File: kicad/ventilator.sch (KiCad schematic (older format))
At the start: 44 parts, among them J1 Conn_01x02, J2 Conn_01x02, J3 Conn_01x02, J4 Conn_01x02, J5 Conn_01x02, J6 Conn_01x02, Q1 IRLIZ44NPBF, Q2 IRLIZ44NPBF, Q3 IRLIZ44NPBF, Q4 IRLIZ44NPBF, Q5 IRLIZ44NPBF, Q6 IRLIZ44NPBF

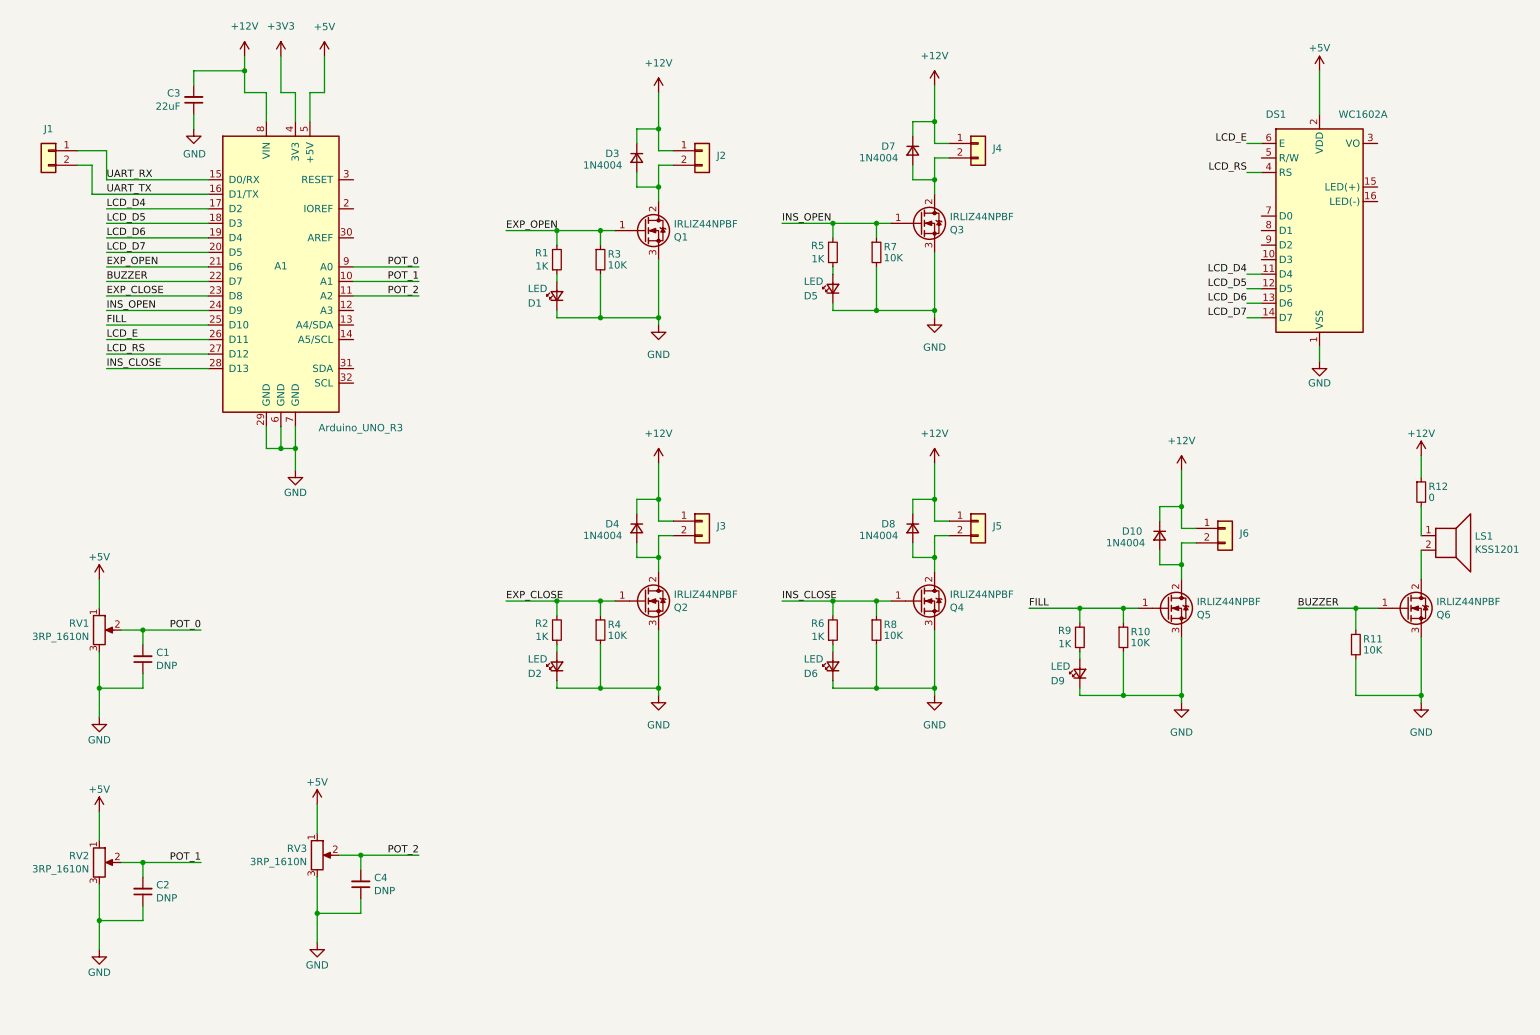
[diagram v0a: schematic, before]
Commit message: modifies schematic with new pin mapping
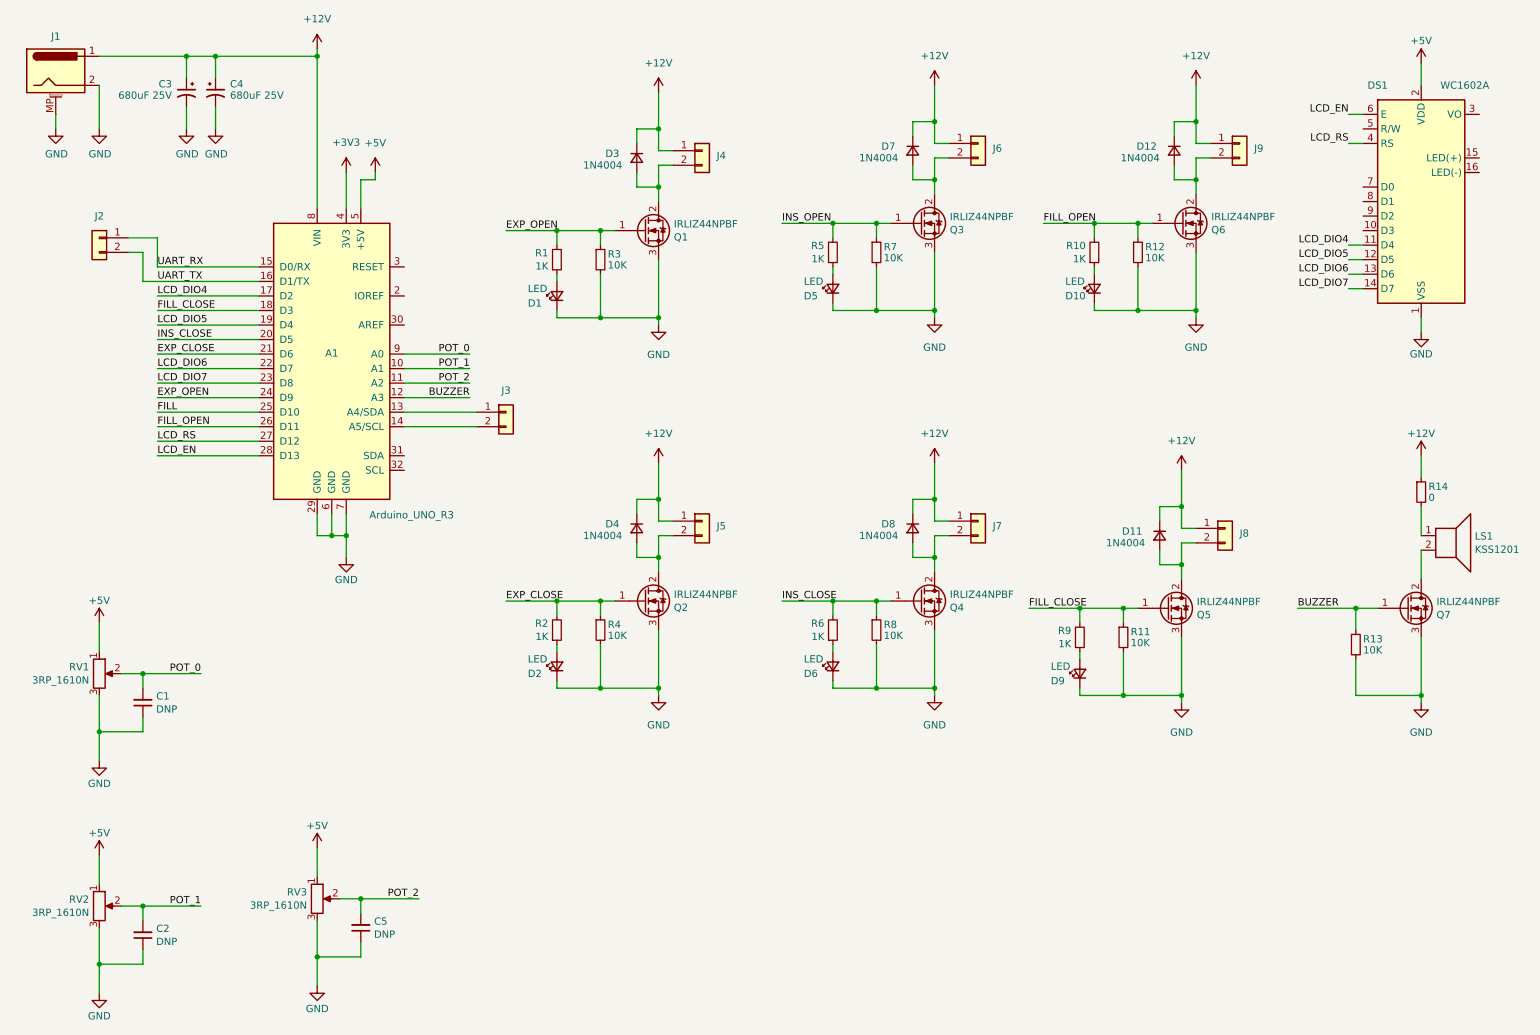
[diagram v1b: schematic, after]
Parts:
- removed C3: 22uF, Capacitor_THT:C_Radial_D6.3mm_H5.0mm_P2.50mm, symbol Device:C_Small
- added C3, C4: 680uF 25V, Capacitor_THT:CP_Radial_D10.0mm_P5.00mm, symbol Device:CP1_Small
- added D10: LED, LED_THT:LED_D5.0mm, symbol Device:LED_Small
- added D12: 1N4004, Diode_THT:D_DO-41_SOD81_P7.62mm_Horizontal, symbol Device:D_Small
- added J1: Barrel_Jack_MountingPin, symbol Connector:Barrel_Jack_MountingPin
- added J3, J9: Conn_01x02, Connector_Phoenix_MSTB:PhoenixContact_MSTBA_2,5_2-G-5,08_1x02_P5.08mm_Horizontal, symbol Connector_Generic:Conn_01x02
- added Q6: IRLIZ44NPBF, Package_TO_SOT_THT:TO-220-3_Vertical, symbol Device:Q_NMOS_GDS
- added R10: 1K, Resistor_THT:R_Axial_DIN0207_L6.3mm_D2.5mm_P7.62mm_Horizontal, symbol Device:R_Small
- added R12: 10K, Resistor_THT:R_Axial_DIN0207_L6.3mm_D2.5mm_P7.62mm_Horizontal, symbol Device:R_Small
- renumbered C4 to C5, D10 to D11, J1 to J2, J2 to J4, J3 to J5, J4 to J6, J5 to J7, J6 to J8, Q6 to Q7, R10 to R11, R11 to R13, R12 to R14
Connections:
- net +12V: now also C3.1, C4.1, D12.1 (K), J1.1, J9.1 (Pin_1)
- net BUZZER: now also A1.12 (A3); no longer A1.22 (D7)
- net EXP_CLOSE: now also A1.21 (D6); no longer A1.23 (D8)
- net EXP_OPEN: now also A1.24 (D9); no longer A1.21 (D6)
- net FILL: no longer Q5.1 (G), R11.1, R9.2
- net GND: now also C3.2, C4.2, D10.1 (K), J1.2, J1.MP (MountPin), Q6.3 (S), R12.2
- net INS_CLOSE: now also A1.20 (D5); no longer A1.28 (D13)
- net INS_OPEN: no longer A1.24 (D9)
- net at A1.13 (A4/SDA): now also J3.1 (Pin_1)
- net at A1.14 (A5/SCL): now also J3.2 (Pin_2)
- net LCD_D4 renamed LCD_DIO4
- net LCD_D5 renamed FILL_CLOSE
- net FILL_CLOSE: now also Q5.1 (G), R11.1, R9.2; no longer DS1.12 (D5)
- net LCD_D6 renamed LCD_DIO5
- net LCD_DIO5: now also DS1.12 (D5); no longer DS1.13 (D6)
- net LCD_D7 renamed LCD_DIO7
- net LCD_DIO7: now also A1.23 (D8); no longer A1.20 (D5)
- net LCD_E renamed FILL_OPEN
- net FILL_OPEN: now also Q6.1 (G), R10.2, R12.1; no longer DS1.6 (E)
- new net: D10.2 (A), R10.1
- new net: D12.2 (A), J9.2 (Pin_2), Q6.2 (D)
- new net LCD_DIO6: A1.22 (D7), DS1.13 (D6)
- new net LCD_EN: A1.28 (D13), DS1.6 (E)
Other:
- moved on the sheet: A1, C1, C2, C5, DS1, J2, RV1, RV2, RV3

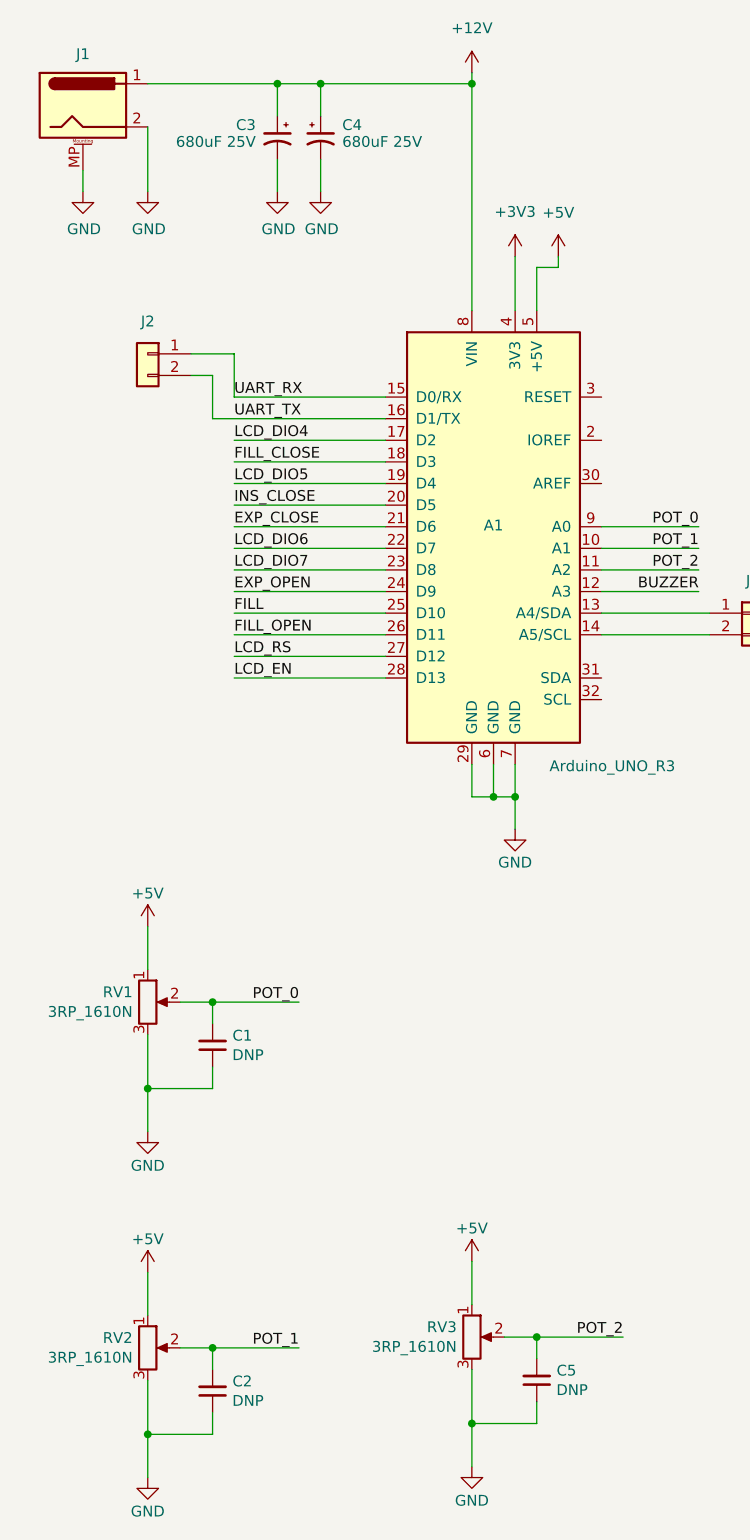
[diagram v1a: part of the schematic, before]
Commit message: finishes basic kicad board layout
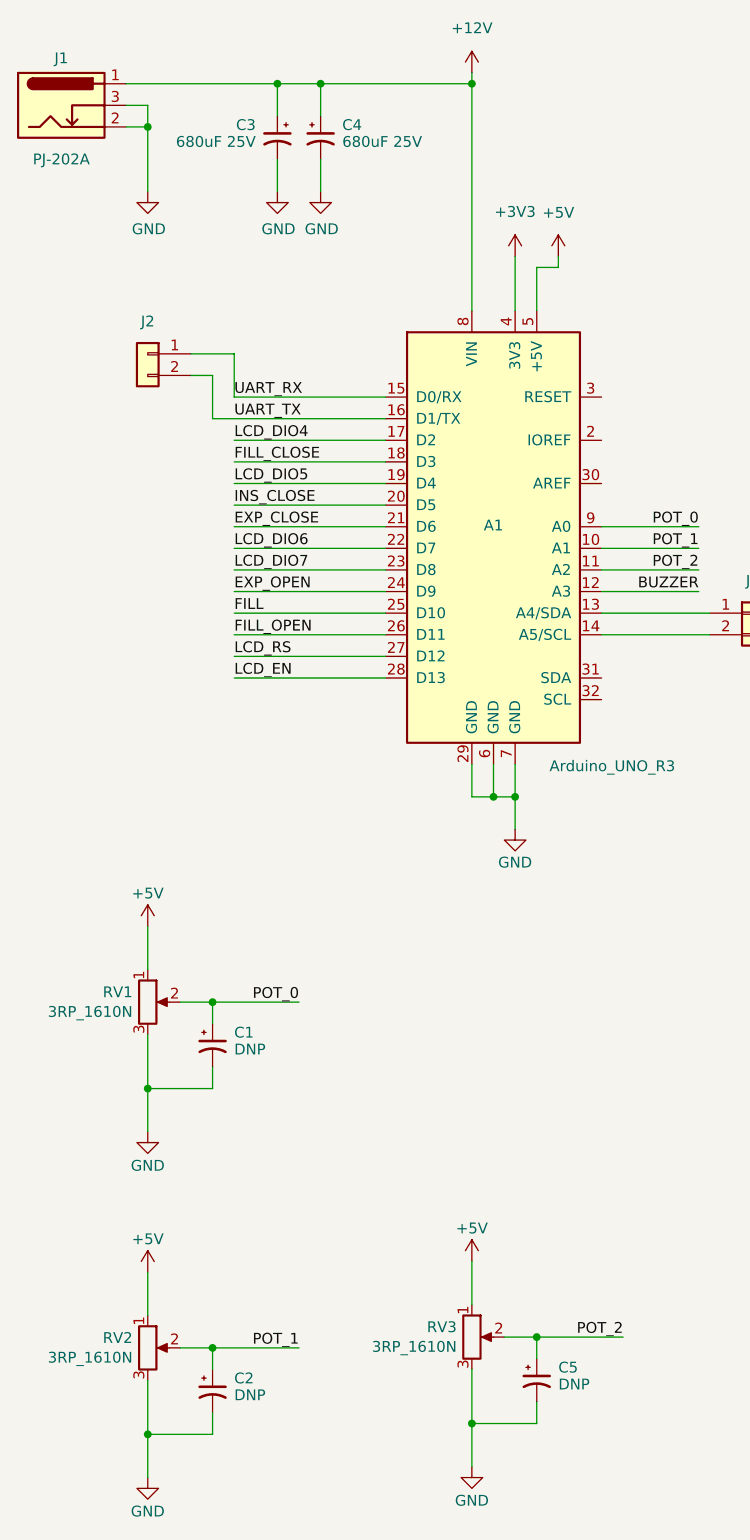
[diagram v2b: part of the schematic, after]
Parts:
- removed C1, C2, C5: DNP, Capacitor_THT:C_Radial_D6.3mm_H5.0mm_P2.50mm, symbol Device:C_Small
- removed J1: Barrel_Jack_MountingPin, symbol Connector:Barrel_Jack_MountingPin
- added C1, C2, C5: DNP, Capacitor_THT:CP_Radial_D6.3mm_P2.50mm, symbol Device:CP1_Small
- added J1: PJ-202A, Connector_BarrelJack:BarrelJack_Horizontal, symbol Connector:Barrel_Jack_Switch
- J2, J3: footprint Connector_Phoenix_MSTB:PhoenixContact_MSTBA_2,5_2-G-5,08_1x02_P5.08mm_Horizontal -> Connector_PinHeader_2.54mm:PinHeader_1x02_P2.54mm_Vertical
- J4, J5, J6, J7, J8, J9: footprint Connector_Phoenix_MSTB:PhoenixContact_MSTBA_2,5_2-G-5,08_1x02_P5.08mm_Horizontal -> TerminalBlock_Phoenix:TerminalBlock_Phoenix_MKDS-1,5-2-5.08_1x02_P5.08mm_Horizontal
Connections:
- net +12V: now also J1.1
- net GND: now also C1.2, C2.2, C5.2, J1.2, J1.3
- net POT_0: now also C1.1
- net POT_1: now also C2.1
- net POT_2: now also C5.1
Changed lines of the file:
@@
 Connection ~ 2000 800
 Connection ~ 2700 800
-Wire Wire Line
-	900  1200 900  1300
-Wire Wire Line
-	1200 800  1800 800
+Connection ~ 1200 1000
+Wire Wire Line
+	1100 800  1800 800
+Wire Wire Line
+	1100 900  1200 900
+Wire Wire Line
+	1100 1000 1200 1000
+Wire Wire Line
+	1200 900  1200 1000
 Wire Wire Line
 	1200 1000 1200 1300
@@
 $EndComp
 $Comp
-L power:GND #PWR01
-U 1 1 5E8818C1
-P 900 1300
-F 0 "#PWR01" H 900 1050 50  0001 C CNN
-F 1 "GND" H 905 1127 50  0000 C CNN
-F 2 "" H 900 1300 50  0001 C CNN
-F 3 "" H 900 1300 50  0001 C CNN
-	1    900  1300
-	1    0    0    -1
-$EndComp
-$Comp
 L power:GND #PWR02
 U 1 1 5E88DD14
@@
 $EndComp
 $Comp
+L Device:CP1_Small C1
+U 1 1 5E861DB0
+P 1500 5250
+F 0 "C1" H 1600 5309 50  0000 L CNN
+F 1 "DNP" H 1600 5231 50  0000 L CNN
+F 2 "Capacitor_THT:CP_Radial_D6.3mm_P2.50mm" H 1500 5250 50  0001 C CNN
+F 3 "~" H 1500 5250 50  0001 C CNN
+	1    1500 5250
+	1    0    0    -1
+$EndComp
+$Comp
+L Device:CP1_Small C2
+U 1 1 5E865C76
+P 1500 6850
+F 0 "C2" H 1600 6909 50  0000 L CNN
+F 1 "DNP" H 1600 6831 50  0000 L CNN
+F 2 "Capacitor_THT:CP_Radial_D6.3mm_P2.50mm" H 1500 6850 50  0001 C CNN
+F 3 "~" H 1500 6850 50  0001 C CNN
+	1    1500 6850
+	1    0    0    -1
+$EndComp
+$Comp
 L Device:CP1_Small C3
 U 1 1 5E882863
@@
 $EndComp
 $Comp
-L Device:C_Small C1
-U 1 1 5E84D8F9
-P 1500 5250
-F 0 "C1" H 1592 5205 50  0000 L CNN
-F 1 "DNP" H 1591 5295 50  0000 L CNN
-F 2 "Capacitor_THT:C_Radial_D6.3mm_H5.0mm_P2.50mm" H 1500 5250 50  0001 C CNN
-F 3 "~" H 1500 5250 50  0001 C CNN
-	1    1500 5250
-	1    0    0    1
-$EndComp
-$Comp
-L Device:C_Small C2
-U 1 1 5E857062
-P 1500 6850
-F 0 "C2" H 1592 6805 50  0000 L CNN
-F 1 "DNP" H 1591 6895 50  0000 L CNN
-F 2 "Capacitor_THT:C_Radial_D6.3mm_H5.0mm_P2.50mm" H 1500 6850 50  0001 C CNN
-F 3 "~" H 1500 6850 50  0001 C CNN
-	1    1500 6850
-	1    0    0    1
-$EndComp
-$Comp
-L Device:C_Small C5
-U 1 1 5E8610A5
+L Device:CP1_Small C5
+U 1 1 5E867241
 P 3000 6800
-F 0 "C5" H 3092 6755 50  0000 L CNN
-F 1 "DNP" H 3091 6845 50  0000 L CNN
-F 2 "Capacitor_THT:C_Radial_D6.3mm_H5.0mm_P2.50mm" H 3000 6800 50  0001 C CNN
+F 0 "C5" H 3100 6859 50  0000 L CNN
+F 1 "DNP" H 3100 6781 50  0000 L CNN
+F 2 "Capacitor_THT:CP_Radial_D6.3mm_P2.50mm" H 3000 6800 50  0001 C CNN
 F 3 "~" H 3000 6800 50  0001 C CNN
 	1    3000 6800
-	1    0    0    1
+	1    0    0    -1
 $EndComp
 $Comp
@@
 F 0 "J2" H 1200 2200 50  0000 C CNN
 F 1 "Conn_01x02" H 1120 2176 50  0001 C CNN
-F 2 "Connector_Phoenix_MSTB:PhoenixContact_MSTBA_2,5_2-G-5,08_1x02_P5.08mm_Horizontal" H 1200 2050 50  0001 C CNN
+F 2 "Connector_PinHeader_2.54mm:PinHeader_1x02_P2.54mm_Vertical" H 1200 2050 50  0001 C CNN
 F 3 "~" H 1200 2050 50  0001 C CNN
 	1    1200 2050
@@
 F 0 "J3" H 4000 3400 50  0000 C CNN
 F 1 "Conn_01x02" H 3920 3376 50  0001 C CNN
-F 2 "Connector_Phoenix_MSTB:PhoenixContact_MSTBA_2,5_2-G-5,08_1x02_P5.08mm_Horizontal" H 4000 3250 50  0001 C CNN
+F 2 "Connector_PinHeader_2.54mm:PinHeader_1x02_P2.54mm_Vertical" H 4000 3250 50  0001 C CNN
 F 3 "~" H 4000 3250 50  0001 C CNN
 	1    4000 3250
@@
 F 0 "J4" H 5450 1416 50  0000 L CNN
 F 1 "Conn_01x02" H 5430 1549 50  0001 L CNN
-F 2 "Connector_Phoenix_MSTB:PhoenixContact_MSTBA_2,5_2-G-5,08_1x02_P5.08mm_Horizontal" H 5350 1450 50  0001 C CNN
+F 2 "TerminalBlock_Phoenix:TerminalBlock_Phoenix_MKDS-1,5-2-5.08_1x02_P5.08mm_Horizontal" H 5350 1450 50  0001 C CNN
 F 3 "~" H 5350 1450 50  0001 C CNN
 	1    5350 1450
@@
 F 0 "J5" H 5450 3966 50  0000 L CNN
 F 1 "Conn_01x02" H 5430 4099 50  0001 L CNN
-F 2 "Connector_Phoenix_MSTB:PhoenixContact_MSTBA_2,5_2-G-5,08_1x02_P5.08mm_Horizontal" H 5350 4000 50  0001 C CNN
+F 2 "TerminalBlock_Phoenix:TerminalBlock_Phoenix_MKDS-1,5-2-5.08_1x02_P5.08mm_Horizontal" H 5350 4000 50  0001 C CNN
 F 3 "~" H 5350 4000 50  0001 C CNN
 	1    5350 4000
@@
 F 0 "J6" H 7350 1366 50  0000 L CNN
 F 1 "Conn_01x02" H 7330 1499 50  0001 L CNN
-F 2 "Connector_Phoenix_MSTB:PhoenixContact_MSTBA_2,5_2-G-5,08_1x02_P5.08mm_Horizontal" H 7250 1400 50  0001 C CNN
+F 2 "TerminalBlock_Phoenix:TerminalBlock_Phoenix_MKDS-1,5-2-5.08_1x02_P5.08mm_Horizontal" H 7250 1400 50  0001 C CNN
 F 3 "~" H 7250 1400 50  0001 C CNN
 	1    7250 1400
@@
 F 0 "J7" H 7350 3966 50  0000 L CNN
 F 1 "Conn_01x02" H 7330 4099 50  0001 L CNN
-F 2 "Connector_Phoenix_MSTB:PhoenixContact_MSTBA_2,5_2-G-5,08_1x02_P5.08mm_Horizontal" H 7250 4000 50  0001 C CNN
+F 2 "TerminalBlock_Phoenix:TerminalBlock_Phoenix_MKDS-1,5-2-5.08_1x02_P5.08mm_Horizontal" H 7250 4000 50  0001 C CNN
 F 3 "~" H 7250 4000 50  0001 C CNN
 	1    7250 4000
@@
 F 0 "J8" H 9050 4016 50  0000 L CNN
 F 1 "Conn_01x02" H 9030 4149 50  0001 L CNN
-F 2 "Connector_Phoenix_MSTB:PhoenixContact_MSTBA_2,5_2-G-5,08_1x02_P5.08mm_Horizontal" H 8950 4050 50  0001 C CNN
+F 2 "TerminalBlock_Phoenix:TerminalBlock_Phoenix_MKDS-1,5-2-5.08_1x02_P5.08mm_Horizontal" H 8950 4050 50  0001 C CNN
 F 3 "~" H 8950 4050 50  0001 C CNN
 	1    8950 4050
@@
 F 0 "J9" H 9150 1366 50  0000 L CNN
 F 1 "Conn_01x02" H 9130 1499 50  0001 L CNN
-F 2 "Connector_Phoenix_MSTB:PhoenixContact_MSTBA_2,5_2-G-5,08_1x02_P5.08mm_Horizontal" H 9050 1400 50  0001 C CNN
+F 2 "TerminalBlock_Phoenix:TerminalBlock_Phoenix_MKDS-1,5-2-5.08_1x02_P5.08mm_Horizontal" H 9050 1400 50  0001 C CNN
 F 3 "~" H 9050 1400 50  0001 C CNN
 	1    9050 1400
@@
 $EndComp
 $Comp
+L Connector:Barrel_Jack_Switch J1
+U 1 1 5E85015B
+P 800 900
+F 0 "J1" H 800 1118 50  0000 C CNN
+F 1 "PJ-202A" H 800 650 50  0000 C CNN
+F 2 "Connector_BarrelJack:BarrelJack_Horizontal" H 850 860 50  0001 C CNN
+F 3 "~" H 850 860 50  0001 C CNN
+	1    800  900
+	1    0    0    -1
+$EndComp
+$Comp
 L Device:Q_NMOS_GDS Q1
 U 1 1 5E86C9E7
@@
 	1    0    0    -1
 $EndComp
-$Comp
-L Connector:Barrel_Jack_MountingPin J1
-U 1 1 5E87BC82
-P 900 900
-F 0 "J1" H 900 1137 50  0000 C CNN
-F 1 "Barrel_Jack_MountingPin" H 900 1149 50  0001 C CNN
-F 2 "" H 950 860 50  0001 C CNN
-F 3 "~" H 950 860 50  0001 C CNN
-	1    900  900
-	1    0    0    -1
-$EndComp
